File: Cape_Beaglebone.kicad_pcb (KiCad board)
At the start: 2 copper layers, 79.4 x 54.6 mm, 92 parts, among them IC1 MPU-9250, IC10 HMC5883L-TR, IC11 BMP180, IC12 ADS8688IDBT, IC13 L3GD20H, IC2 HX711, IC3 DS3231S, IC4 HX711, IC5 CAT24C256WI-GT3, IC6 AD7793BRUZ, IC7 AD7793BRUZ, IC8 MPU-6500, IC9 LSM303D, J1 Conn_01x04, J10 Conn_01x04, J11 Conn_01x06, J12 Conn_01x04, J13 Conn_01x04, J14 Conn_01x04, J15 Conn_01x04, J16 Conn_01x06, J2 Conn_01x04, J3 Conn_01x02, J4 Conn_01x06, J5 M_WP, J6 Conn_01x06, J7 Conn_01x04, J8 Conn_01x04, J9 Conn_01x04, P8 BeagleBone_Black_Header, P9 BeagleBone_Black_Header, Q1 BC807, Q2 BC807, SW1 SW_DIP_x02, U1 4525DO-DS5AI001DP

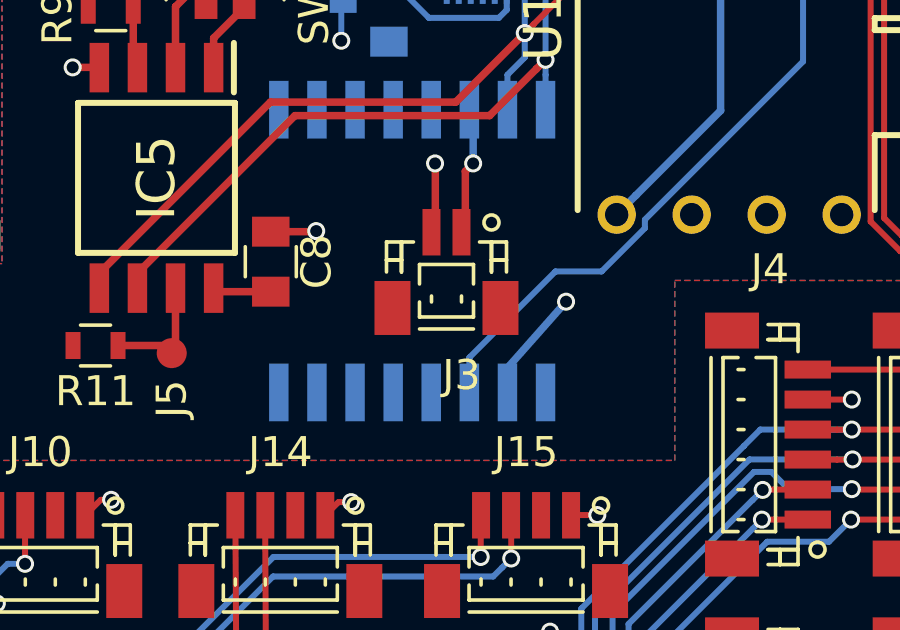
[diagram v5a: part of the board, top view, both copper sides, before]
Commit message: Conector bateiira RTC
Troca do conector da bateria do RTC de JSH SH para o JST GH. Pois não tinha o SH disponivel para comprar.
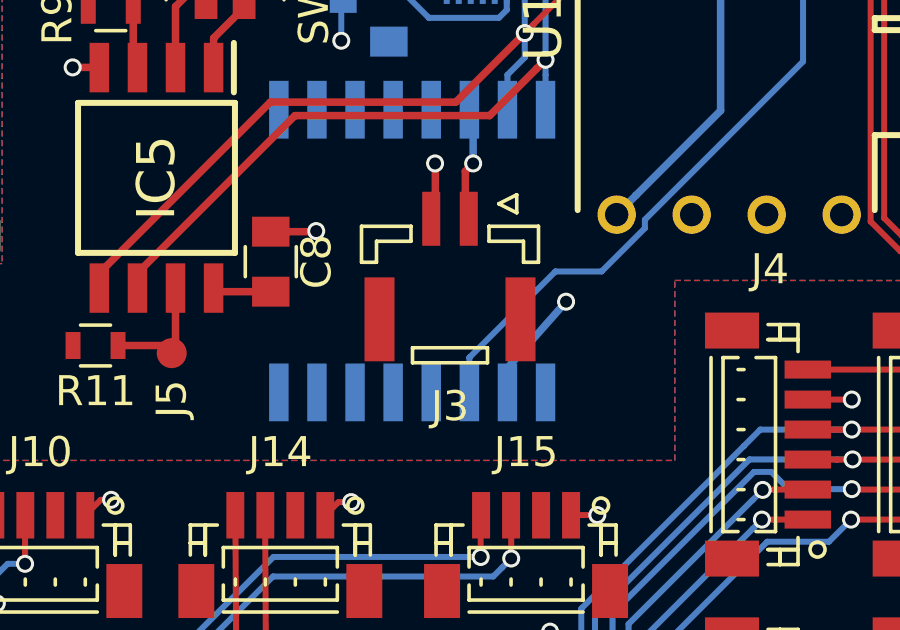
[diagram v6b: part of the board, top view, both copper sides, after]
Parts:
- J3: footprint Connectors_JST:JST_SH_BM02B-SRSS-TB_02x1.00mm_Straight -> Connectors_JST:JST_GH_BM02B-GHS-TBT_02x1.25mm_Straight
- moved J3 0.12 mm to (173.6, 69.6)
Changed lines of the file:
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@@
   (page A4)
   (layers
-    (0 F.Cu power)
+    (0 F.Cu power hide)
     (31 B.Cu signal hide)
-    (33 F.Adhes user)
+    (33 F.Adhes user hide)
     (35 F.Paste user hide)
     (36 B.SilkS user)
     (37 F.SilkS user)
-    (38 B.Mask user hide)
+    (38 B.Mask user)
     (39 F.Mask user)
     (44 Edge.Cuts user)
     (45 Margin user hide)
-    (46 B.CrtYd user)
-    (47 F.CrtYd user)
+    (46 B.CrtYd user hide)
+    (47 F.CrtYd user hide)
   )
   (setup
@@
     (visible_elements 7FFFFFFF)
     (pcbplotparams
-      (layerselection 0x01030_ffffffff)
+      (layerselection 0x010f0_ffffffff)
       (usegerberextensions false)
       (usegerberattributes false)
@@
       (psa4output false)
       (plotreference true)
-      (plotvalue true)
+      (plotvalue false)
       (plotinvisibletext false)
       (padsonsilk false)
@@
     (add_net "Net-(IC1-Pad9)")
   )
+  (module Connectors_JST:JST_GH_BM02B-GHS-TBT_02x1.25mm_Straight (layer F.Cu)
+    (at 173.61 69.615 180)
+    (descr "JST GH series connector, BM02B-GHS-TBT, top entry type")
+    (tags "connector jst GH SMT top vertical entry 1.25mm pitch")
+    (attr smd)
+    (fp_text reference J3 (at 0 -4.575 180) (layer F.SilkS)
+      (effects (font (size 1 1) (thickness 0.15)))
+    )
+    (fp_text value Conn_01x02 (at 0 3.675 180) (layer F.Fab)
+      (effects (font (size 1 1) (thickness 0.15)))
+    )
+    (fp_text user %R (at 0 -1.825 180) (layer F.Fab)
+      (effects (font (size 1 1) (thickness 0.15)))
+    )
+    (fp_line (start -2.85 1.3) (end -2.85 -2.95) (layer F.Fab) (width 0.1))
+    (fp_line (start -2.85 -2.95) (end 2.85 -2.95) (layer F.Fab) (width 0.1))
+    (fp_line (start 2.85 -2.95) (end 2.85 1.3) (layer F.Fab) (width 0.1))
+    (fp_line (start 2.85 1.3) (end -2.85 1.3) (layer F.Fab) (width 0.1))
+    (fp_line (start -1.25 -3.125) (end 1.25 -3.125) (layer F.SilkS) (width 0.12))
+    (fp_line (start 1.25 -3.125) (end 1.25 -2.625) (layer F.SilkS) (width 0.12))
+    (fp_line (start 1.25 -2.625) (end -1.25 -2.625) (layer F.SilkS) (width 0.12))
+    (fp_line (start -1.25 -2.625) (end -1.25 -3.125) (layer F.SilkS) (width 0.12))
+    (fp_line (start -2.95 0.225) (end -2.95 1.425) (layer F.SilkS) (width 0.12))
+    (fp_line (start -2.95 1.425) (end -1.3 1.425) (layer F.SilkS) (width 0.12))
+    (fp_line (start -1.3 1.425) (end -1.3 0.925) (layer F.SilkS) (width 0.12))
+    (fp_line (start -1.3 0.925) (end -2.45 0.925) (layer F.SilkS) (width 0.12))
+    (fp_line (start -2.45 0.925) (end -2.45 0.225) (layer F.SilkS) (width 0.12))
+    (fp_line (start -2.45 0.225) (end -2.95 0.225) (layer F.SilkS) (width 0.12))
+    (fp_line (start 2.95 0.225) (end 2.95 1.425) (layer F.SilkS) (width 0.12))
+    (fp_line (start 2.95 1.425) (end 1.3 1.425) (layer F.SilkS) (width 0.12))
+    (fp_line (start 1.3 1.425) (end 1.3 0.925) (layer F.SilkS) (width 0.12))
+    (fp_line (start 1.3 0.925) (end 2.45 0.925) (layer F.SilkS) (width 0.12))
+    (fp_line (start 2.45 0.925) (end 2.45 0.225) (layer F.SilkS) (width 0.12))
+    (fp_line (start 2.45 0.225) (end 2.95 0.225) (layer F.SilkS) (width 0.12))
+    (fp_line (start -1.625 2.175) (end -2.225 2.475) (layer F.SilkS) (width 0.12))
+    (fp_line (start -2.225 2.475) (end -2.225 1.875) (layer F.SilkS) (width 0.12))
+    (fp_line (start -2.225 1.875) (end -1.625 2.175) (layer F.SilkS) (width 0.12))
+    (fp_line (start -1.625 2.175) (end -2.225 2.475) (layer F.Fab) (width 0.1))
+    (fp_line (start -2.225 2.475) (end -2.225 1.875) (layer F.Fab) (width 0.1))
+    (fp_line (start -2.225 1.875) (end -1.625 2.175) (layer F.Fab) (width 0.1))
+    (fp_line (start -0.875 -0.325) (end -0.875 -0.825) (layer F.Fab) (width 0.1))
+    (fp_line (start -0.875 -0.825) (end -0.375 -0.825) (layer F.Fab) (width 0.1))
+    (fp_line (start -0.375 -0.825) (end -0.375 -0.325) (layer F.Fab) (width 0.1))
+    (fp_line (start -0.375 -0.325) (end -0.875 -0.325) (layer F.Fab) (width 0.1))
+    (fp_line (start 0.375 -0.325) (end 0.375 -0.825) (layer F.Fab) (width 0.1))
+    (fp_line (start 0.375 -0.825) (end 0.875 -0.825) (layer F.Fab) (width 0.1))
+    (fp_line (start 0.875 -0.825) (end 0.875 -0.325) (layer F.Fab) (width 0.1))
+    (fp_line (start 0.875 -0.325) (end 0.375 -0.325) (layer F.Fab) (width 0.1))
+    (fp_line (start -3.35 3.05) (end -3.35 -3.6) (layer F.CrtYd) (width 0.05))
+    (fp_line (start -3.35 -3.6) (end 3.35 -3.6) (layer F.CrtYd) (width 0.05))
+    (fp_line (start 3.35 -3.6) (end 3.35 3.05) (layer F.CrtYd) (width 0.05))
+    (fp_line (start 3.35 3.05) (end -3.35 3.05) (layer F.CrtYd) (width 0.05))
+    (pad 1 smd rect (at -0.625 1.675 180) (size 0.6 1.8) (layers F.Cu F.Paste F.Mask)
+      (net 60 "Net-(IC3-Pad14)"))
+    (pad 2 smd rect (at 0.625 1.675 180) (size 0.6 1.8) (layers F.Cu F.Paste F.Mask)
+      (net 1 GNDD))
+    (pad "" smd rect (at 2.35 -1.675 180) (size 1 2.8) (layers F.Cu F.Paste F.Mask))
+    (pad "" smd rect (at -2.35 -1.675 180) (size 1 2.8) (layers F.Cu F.Paste F.Mask))
+  )
   (module complementos:net_tie2 (layer B.Cu)
     (at 136.17 71.416 90)
@@
       (offset (xyz 0 1.5 0))
       (scale (xyz 1 1 1))
-      (rotate (xyz -90 0 0))
-    )
-  )
-  (module Connectors_JST:JST_SH_BM02B-SRSS-TB_02x1.00mm_Straight (layer F.Cu)
-    (at 173.492995 69.651104 180)
-    (descr http://www.jst-mfg.com/product/pdf/eng/eSH.pdf)
-    (tags "connector jst sh")
-    (attr smd)
-    (fp_text reference J3 (at -0.5 -3.5 180) (layer F.SilkS)
-      (effects (font (size 1 1) (thickness 0.15)))
-    )
-    (fp_text value Conn_01x02 (at 0 3.5 180) (layer F.Fab)
-      (effects (font (size 1 1) (thickness 0.15)))
-    )
-    (fp_circle (center -1.5 1.5875) (end -1.25 1.5875) (layer F.SilkS) (width 0.12))
-    (fp_line (start -0.9 -1.9625) (end 0.9 -1.9625) (layer F.SilkS) (width 0.12))
-    (fp_line (start -2 -0.0625) (end -2 0.9375) (layer F.SilkS) (width 0.12))
-    (fp_line (start -2 0.9375) (end -1.1 0.9375) (layer F.SilkS) (width 0.12))
-    (fp_line (start -1.5 0.9375) (end -1.5 -0.0625) (layer F.SilkS) (width 0.12))
-    (fp_line (start -1.5 -0.0625) (end -1.5 -0.0625) (layer F.SilkS) (width 0.12))
-    (fp_line (start -1.5 -0.0625) (end -1.5 0.9375) (layer F.SilkS) (width 0.12))
-    (fp_line (start -1.5 0.9375) (end -1.5 0.9375) (layer F.SilkS) (width 0.12))
-    (fp_line (start -1.5 0.3375) (end -1.5 0.3375) (layer F.SilkS) (width 0.12))
-    (fp_line (start -1.5 0.3375) (end -2 0.3375) (layer F.SilkS) (width 0.12))
-    (fp_line (start -2 0.3375) (end -2 0.3375) (layer F.SilkS) (width 0.12))
-    (fp_line (start -2 0.3375) (end -1.5 0.3375) (layer F.SilkS) (width 0.12))
-    (fp_line (start 2 -0.0625) (end 2 0.9375) (layer F.SilkS) (width 0.12))
-    (fp_line (start 2 0.9375) (end 1.1 0.9375) (layer F.SilkS) (width 0.12))
-    (fp_line (start 1.5 0.9375) (end 1.5 -0.0625) (layer F.SilkS) (width 0.12))
-    (fp_line (start 1.5 -0.0625) (end 1.5 -0.0625) (layer F.SilkS) (width 0.12))
-    (fp_line (start 1.5 -0.0625) (end 1.5 0.9375) (layer F.SilkS) (width 0.12))
-    (fp_line (start 1.5 0.9375) (end 1.5 0.9375) (layer F.SilkS) (width 0.12))
-    (fp_line (start 1.5 0.3375) (end 1.5 0.3375) (layer F.SilkS) (width 0.12))
-    (fp_line (start 1.5 0.3375) (end 2 0.3375) (layer F.SilkS) (width 0.12))
-    (fp_line (start 2 0.3375) (end 2 0.3375) (layer F.SilkS) (width 0.12))
-    (fp_line (start 2 0.3375) (end 1.5 0.3375) (layer F.SilkS) (width 0.12))
-    (fp_line (start -0.9 -1.0625) (end -0.9 -1.5625) (layer F.SilkS) (width 0.12))
-    (fp_line (start -0.9 -1.5625) (end 0.9 -1.5625) (layer F.SilkS) (width 0.12))
-    (fp_line (start 0.9 -1.5625) (end 0.9 -1.0625) (layer F.SilkS) (width 0.12))
-    (fp_line (start -0.9 -0.4625) (end -0.9 0.1875) (layer F.SilkS) (width 0.12))
-    (fp_line (start -0.9 0.1875) (end 0.9 0.1875) (layer F.SilkS) (width 0.12))
-    (fp_line (start 0.9 0.1875) (end 0.9 -0.4625) (layer F.SilkS) (width 0.12))
-    (fp_line (start -0.5 -1.0625) (end -0.5 -0.8625) (layer F.SilkS) (width 0.12))
-    (fp_line (start 0.5 -1.0625) (end 0.5 -0.8625) (layer F.SilkS) (width 0.12))
-    (fp_line (start -2.9 2.55) (end -2.9 -2.7) (layer F.CrtYd) (width 0.05))
-    (fp_line (start -2.9 -2.7) (end 2.9 -2.7) (layer F.CrtYd) (width 0.05))
-    (fp_line (start 2.9 -2.7) (end 2.9 2.55) (layer F.CrtYd) (width 0.05))
-    (fp_line (start 2.9 2.55) (end -2.9 2.55) (layer F.CrtYd) (width 0.05))
-    (pad 1 smd rect (at -0.5 1.2625 180) (size 0.6 1.55) (layers F.Cu F.Paste F.Mask)
-      (net 60 "Net-(IC3-Pad14)"))
-    (pad 2 smd rect (at 0.5 1.2625 180) (size 0.6 1.55) (layers F.Cu F.Paste F.Mask)
-      (net 1 GNDD))
-    (pad "" smd rect (at -1.8 -1.2625 180) (size 1.2 1.8) (layers F.Cu F.Paste F.Mask))
-    (pad "" smd rect (at 1.8 -1.2625 180) (size 1.2 1.8) (layers F.Cu F.Paste F.Mask))
-    (model ${KIPRJMOD}/componetes/BM02B-SRSS-TB/BM02B-SRSS-TB.STEP
-      (offset (xyz 0 1.5 0))
-      (scale (xyz 1 1 1))
